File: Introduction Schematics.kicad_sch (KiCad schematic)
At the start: 9 parts, among them J1 SD_Card_Receptacle, J2 3.3V & Ground, J3 UART 1, J4 UART 2, J5 I2C 2, J6 I2C 1, J7 SPI, J8 Thrusters, U1 ESP32-S3-WROOM-1

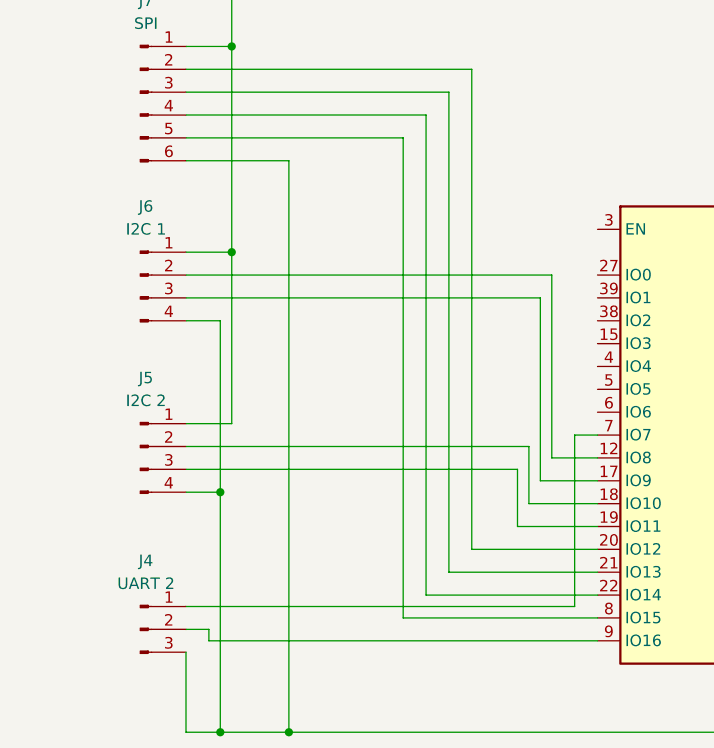
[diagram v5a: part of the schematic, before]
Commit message: Resistors Added for I2C
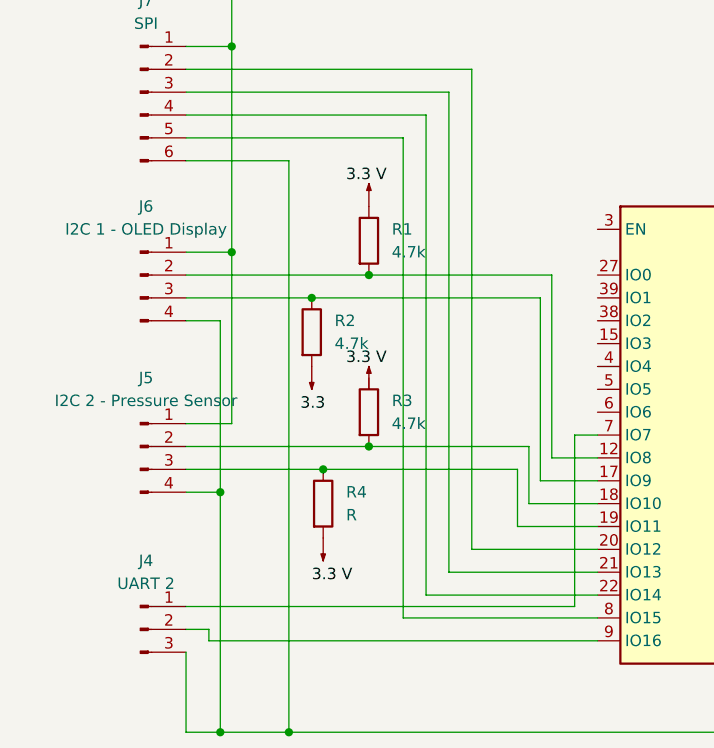
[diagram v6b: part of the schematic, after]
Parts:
- added R1, R2, R3: 4.7k, symbol Device:R
- added R4: R, symbol Device:R
- J5: value I2C 2 -> I2C 2 - Pressure Sensor
- J6: value I2C 1 -> I2C 1 - OLED Display
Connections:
- net at J6.2 (Pin_2), U1.12 (IO8): now also R1.2
- net at J6.3 (Pin_3), U1.17 (IO9): now also R2.1
- net at J5.2 (Pin_2), U1.18 (IO10): now also R3.2
- net at J5.3 (Pin_3), U1.19 (IO11): now also R4.1

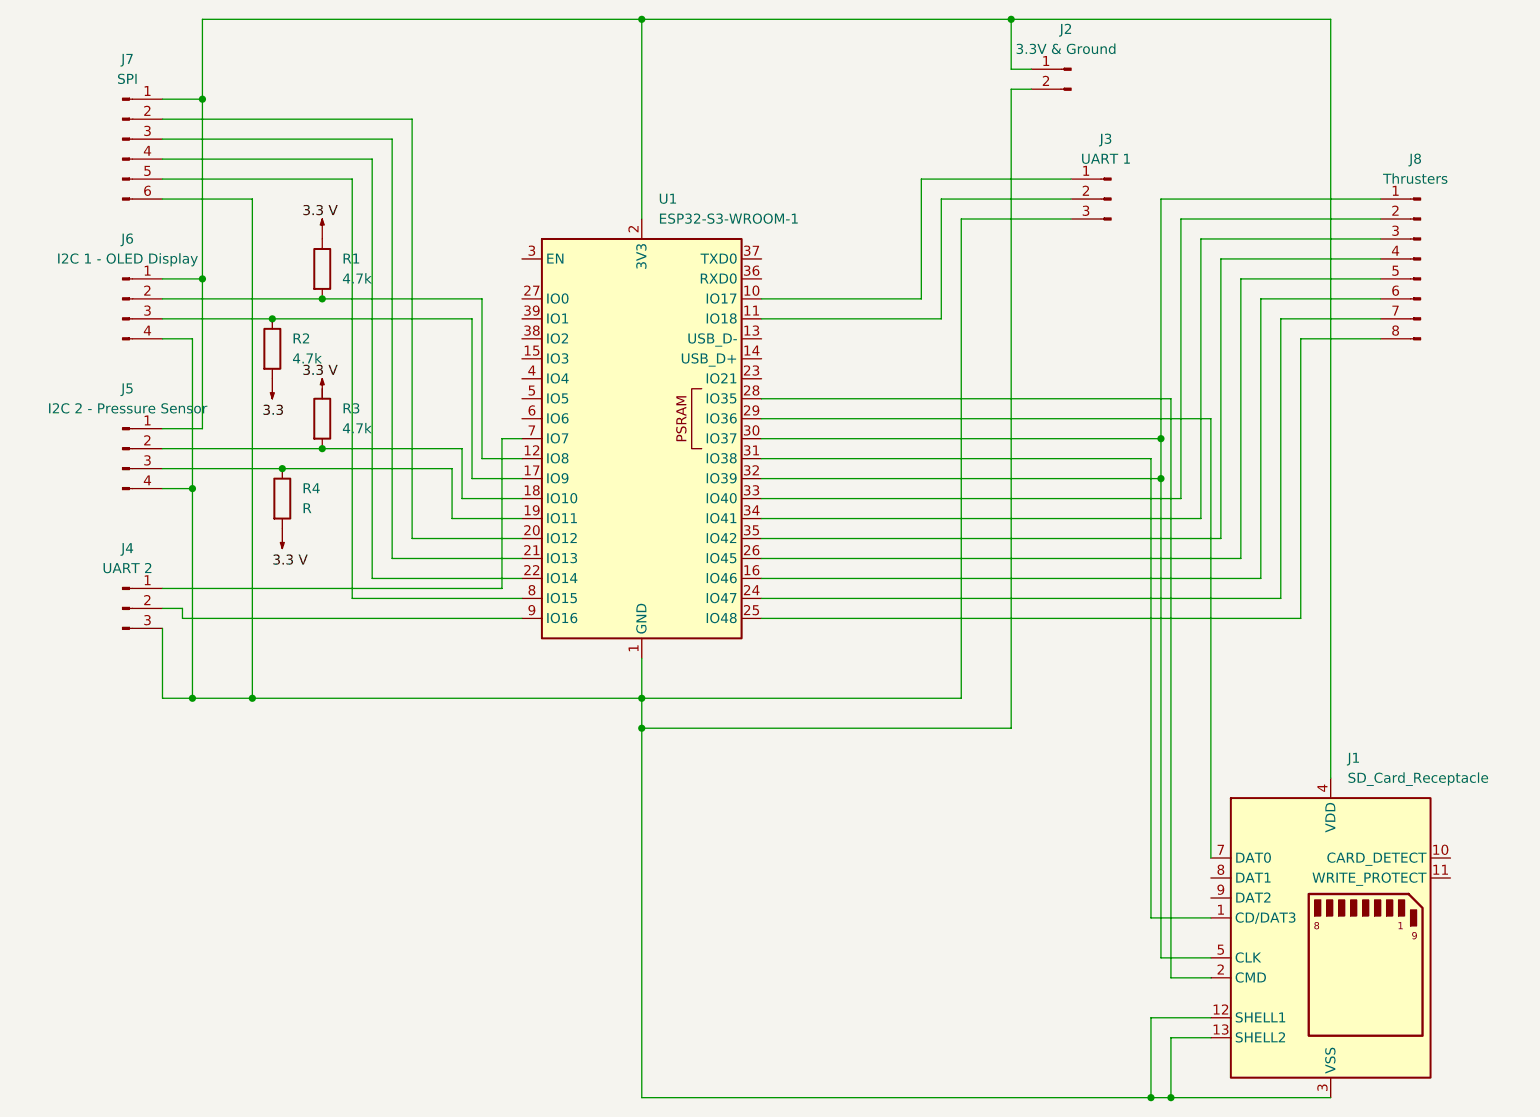
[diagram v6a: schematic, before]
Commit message: En and IO0 added
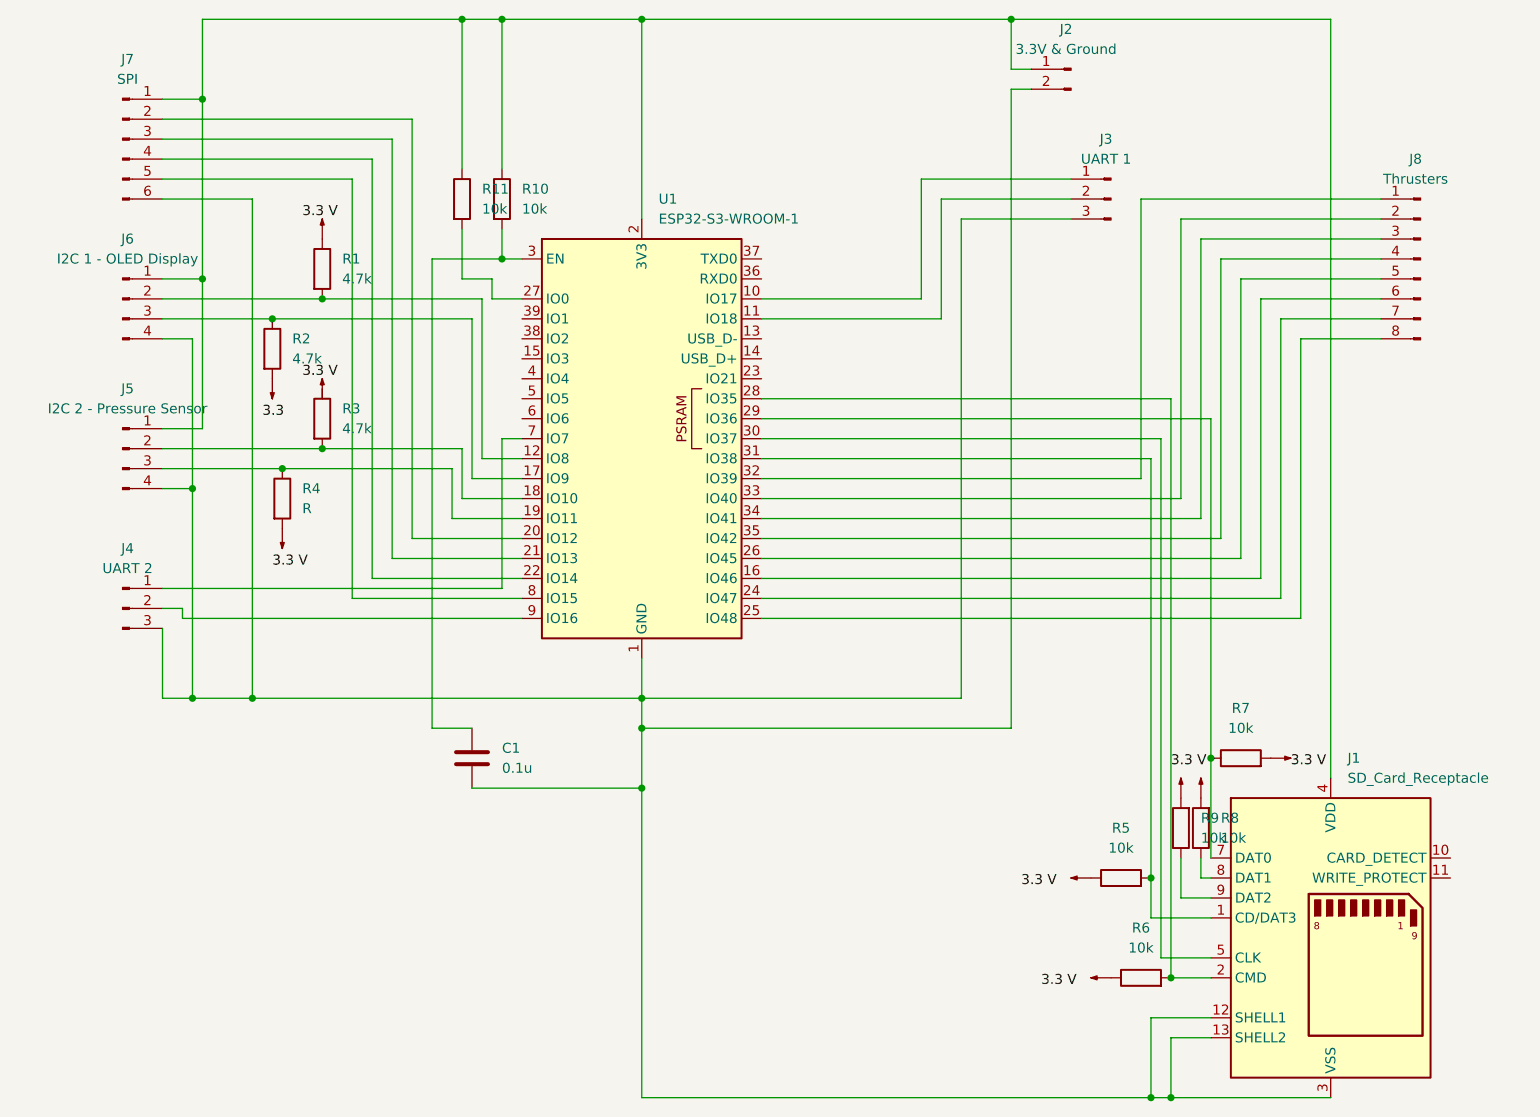
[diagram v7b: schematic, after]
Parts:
- added C1: 0.1u, symbol Device:C
- added R10, R11, R5, R6, R7, R8, R9: 10k, symbol Device:R
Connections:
- net 3.3 V: now also J1.2 (CMD), U1.28 (IO35), R6.2
- net at J1.4 (VDD), J2.1 (Pin_1), J5.1 (Pin_1)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: now also R10.1, R11.1
- net at J1.12 (SHELL1), J1.13 (SHELL2), J1.3 (VSS)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: now also C1.2
- net at J8.1 (Pin_1), U1.32 (IO39): no longer J1.5 (CLK), U1.30 (IO37)
- net at J1.1 (CD/DAT3), U1.31 (IO38): now also R5.2
- net at J1.7 (DAT0), U1.29 (IO36): now also R7.1
- net at J1.8 (DAT1): now also R8.1
- net at J1.9 (DAT2): now also R9.1
- net at U1.27 (IO0): now also R11.2
- net at U1.3 (EN): now also C1.1, R10.2
- new net: J1.5 (CLK), U1.30 (IO37)
